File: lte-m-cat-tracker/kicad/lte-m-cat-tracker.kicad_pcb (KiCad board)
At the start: 2 copper layers, 30 x 35 mm, 33 parts, among them J1 JST-GH-1.25mm-2P, J2 USB-C-16P, SW1 MSK12C02, U1 SIM7080G-M, U2 ESP32-C3, U3 LIS2DW12TR, U4 TP4056, U5 XC6220B331MR-G

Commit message: STEP4a: ANT3→C127629(1206)・C13→C49326798・BOM/CPL作成（2026-06-07）
Co-Authored-By: Claude Sonnet 4.6 <noreply@anthropic.com>
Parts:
- ANT3: value 2450AT18A100 -> RFANT3216120A5T; footprint (none) -> ChipAntenna_1206
- moved ANT3 3.51 mm to (1.80, 19.0)
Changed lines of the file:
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@@
 		(embedded_fonts no)
 	)
-	(footprint ""
+	(footprint "ChipAntenna_1206"
 		(layer "F.Cu")
-		(at 2 22.5)
+		(at 1.8 19.0)
 		(property "Reference" "ANT3"
-			(at 0 -3.5 0)
+			(at 0 -2.0 0)
 			(layer "F.SilkS")
 			(effects
@@
 			)
 		)
-		(property "Value" "2450AT18A100"
-			(at 0 3.5 0)
+		(property "Value" "RFANT3216120A5T"
+			(at 0 2.0 0)
 			(layer "F.Fab")
 			(effects
@@
 			)
 		)
-		(property "Description" ""
+		(property "Description" "2.4GHz chip antenna 1206 Walsin RFANT3216120A5T"
 			(at 0 0 0)
 			(layer "F.Fab")
@@
 		)
 		(duplicate_pad_numbers_are_jumpers no)
-		(fp_line
-			(start -0.2 -0.6)
-			(end -0.2 0.6)
-			(stroke
-				(width 0.12)
-				(type default)
-			)
-			(layer "F.SilkS")
-		)
 		(fp_rect
-			(start -1.2 -0.8)
-			(end 1.2 0.8)
+			(start -1.8 -1.0)
+			(end 1.8 1.0)
 			(stroke
 				(width 0.05)
@@
 		)
 		(fp_rect
-			(start -1 -0.625)
-			(end 1 0.625)
+			(start -1.6 -0.8)
+			(end 1.6 0.8)
 			(stroke
 				(width 0.1)
@@
 		)
 		(pad "1" smd rect
-			(at -0.5 0)
-			(size 0.8 1.25)
+			(at -1.3 0)
+			(size 1.6 1.8)
 			(layers "F.Cu" "F.Mask" "F.Paste")
 			(net "WIFI_ANT")
@@
 		)
 		(pad "2" smd rect
-			(at 0.5 0)
-			(size 0.8 1.25)
+			(at 1.3 0)
+			(size 1.6 1.8)
 			(layers "F.Cu" "F.Mask" "F.Paste")
 			(net "GND")

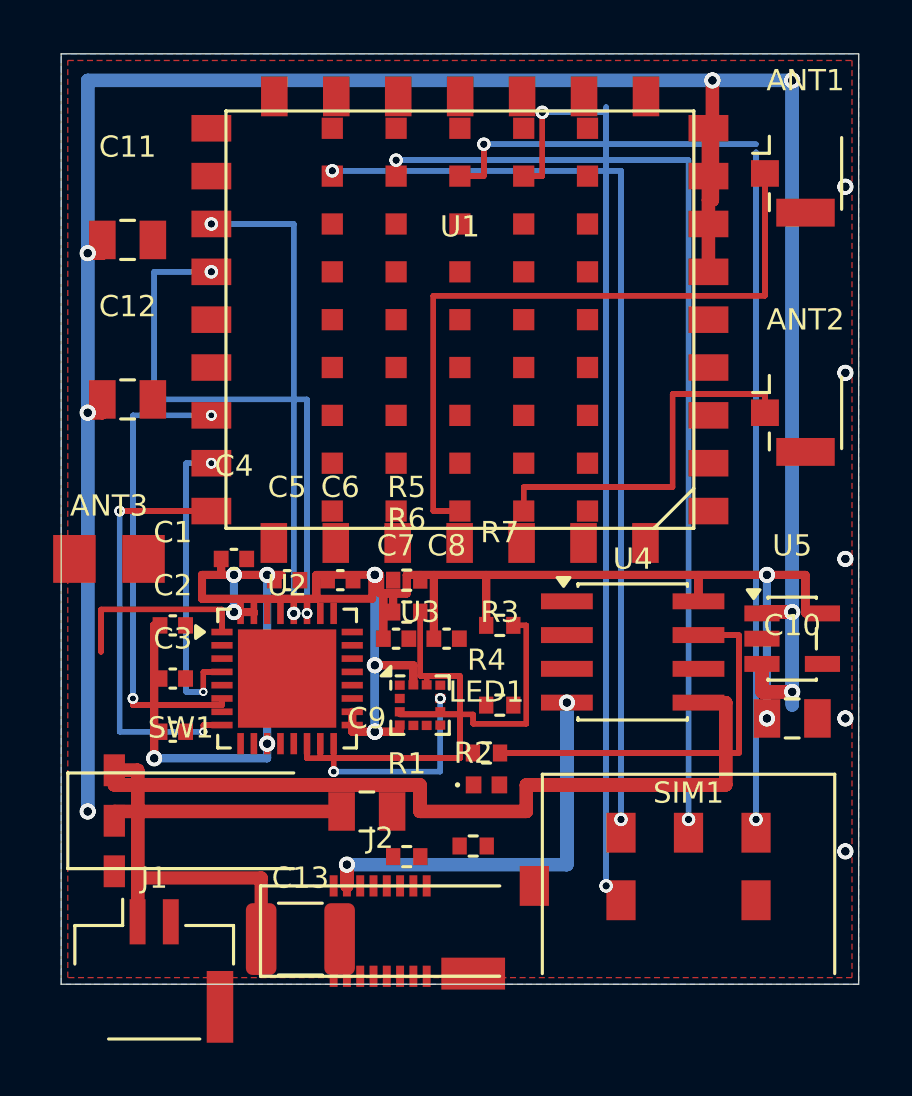
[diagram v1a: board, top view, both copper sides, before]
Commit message: route_pcb_v10.py: +3.3Vバスバイパス y=20.5→y=20.4に修正（短絡0件）
- y=20.5ではU2.pad25/26(y_min=20.65)にtrace y_max=20.65で接触（0mm）
- y=20.4に変更: trace y_max=20.55, pad y_min=20.65 → gap=0.10mm ✅
- y=18.5上方迂回案はU1底行パッド(y=18.4)に接触するため採用不可と判明
- DRC結果: 短絡0件 ✅ / 未配線44件

Co-Authored-By: Claude Sonnet 4.6 <noreply@anthropic.com>
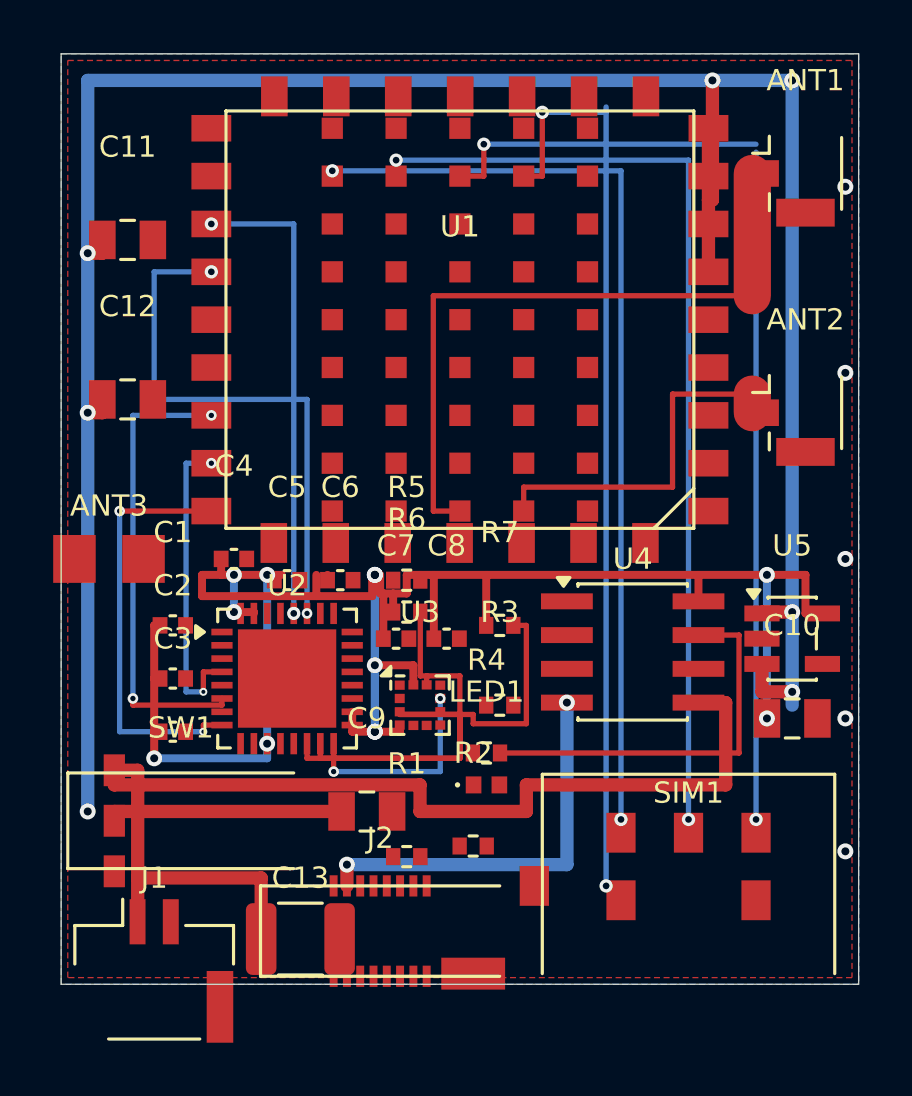
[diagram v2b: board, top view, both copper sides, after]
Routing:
- net VBAT_SW: track 203.8 -> 101.9 mm, vias 14 -> 7
- net +3.3V: track 163.6 -> 82.0 mm, vias 24 -> 12
- net SIM_CLK: track 75.9 -> 37.9 mm, vias 4 -> 2
- net SIM_DATA: track 73.8 -> 36.9 mm, vias 4 -> 2
- net VBAT: track 79.5 -> 43.2 mm
- net SIM_VDD: track 71.9 -> 36.0 mm, vias 4 -> 2
- net SIM_RST: track 71.8 -> 35.9 mm, vias 4 -> 2
- net LTE_ANT: track 52.4 -> 25.7 mm
- net SIM_TXD: track 41.5 -> 20.8 mm, vias 4 -> 2
- net I2C_SCL: track 38.2 -> 19.1 mm
- net SIM_RXD: track 35.5 -> 17.8 mm, vias 4 -> 2
- net SIM_RESETN: track 34.9 -> 17.5 mm, vias 4 -> 2
- net SIM_PWRKEY: track 31.7 -> 15.8 mm, vias 4 -> 2
- net VUSB: track 30.3 -> 15.2 mm, vias 4 -> 2
- net CHRG: track 29.9 -> 14.9 mm
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
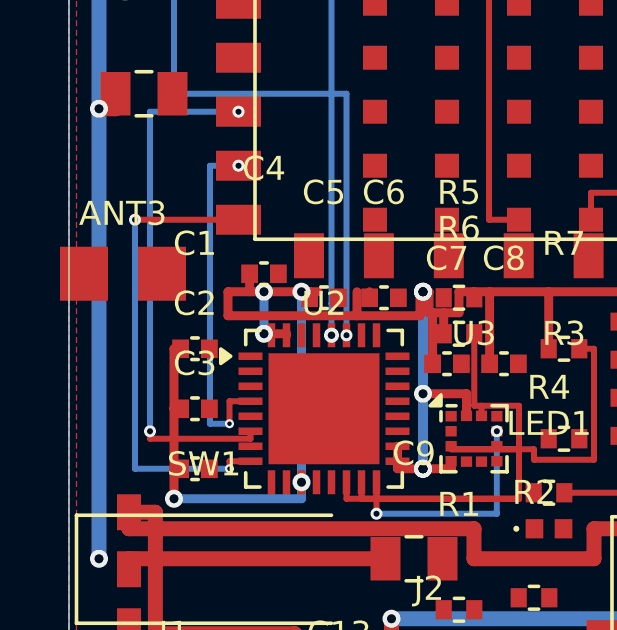
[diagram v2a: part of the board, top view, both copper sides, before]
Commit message: WIFI_ANT配線完了: U2.pad1→ANT3.pad1 F.Cu 0.2mm（短絡0件 ✅ / 未配線10件）
Co-Authored-By: Claude Sonnet 4.6 <noreply@anthropic.com>
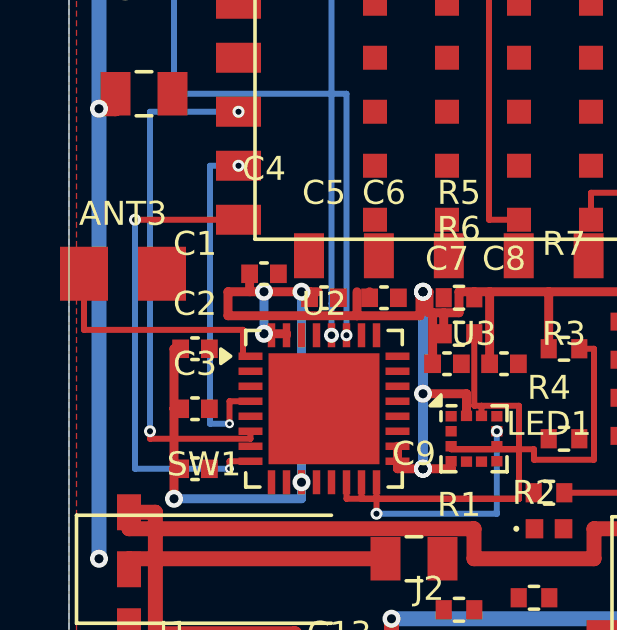
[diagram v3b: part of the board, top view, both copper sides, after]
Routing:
- net WIFI_ANT: track 0.00 -> 8.30 mm
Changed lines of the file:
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@@
 	(segment (start 23.0 12.8) (end 26.0 12.8) (width 0.2) (layer "F.Cu") (net "GNSS_ANT"))
 	(segment (start 26.0 12.8) (end 26.0 13.5) (width 1.4) (layer "F.Cu") (net "GNSS_ANT"))
+	(segment (start 6.05 21.75) (end 5.8 21.75) (width 0.2) (layer "F.Cu") (net "WIFI_ANT"))
+	(segment (start 5.8 21.75) (end 5.8 20.87) (width 0.2) (layer "F.Cu") (net "WIFI_ANT"))
+	(segment (start 5.8 20.87) (end 0.5 20.87) (width 0.2) (layer "F.Cu") (net "WIFI_ANT"))
+	(segment (start 0.5 20.87) (end 0.5 19.0) (width 0.2) (layer "F.Cu") (net "WIFI_ANT"))
 	(zone
 		(net "GND")

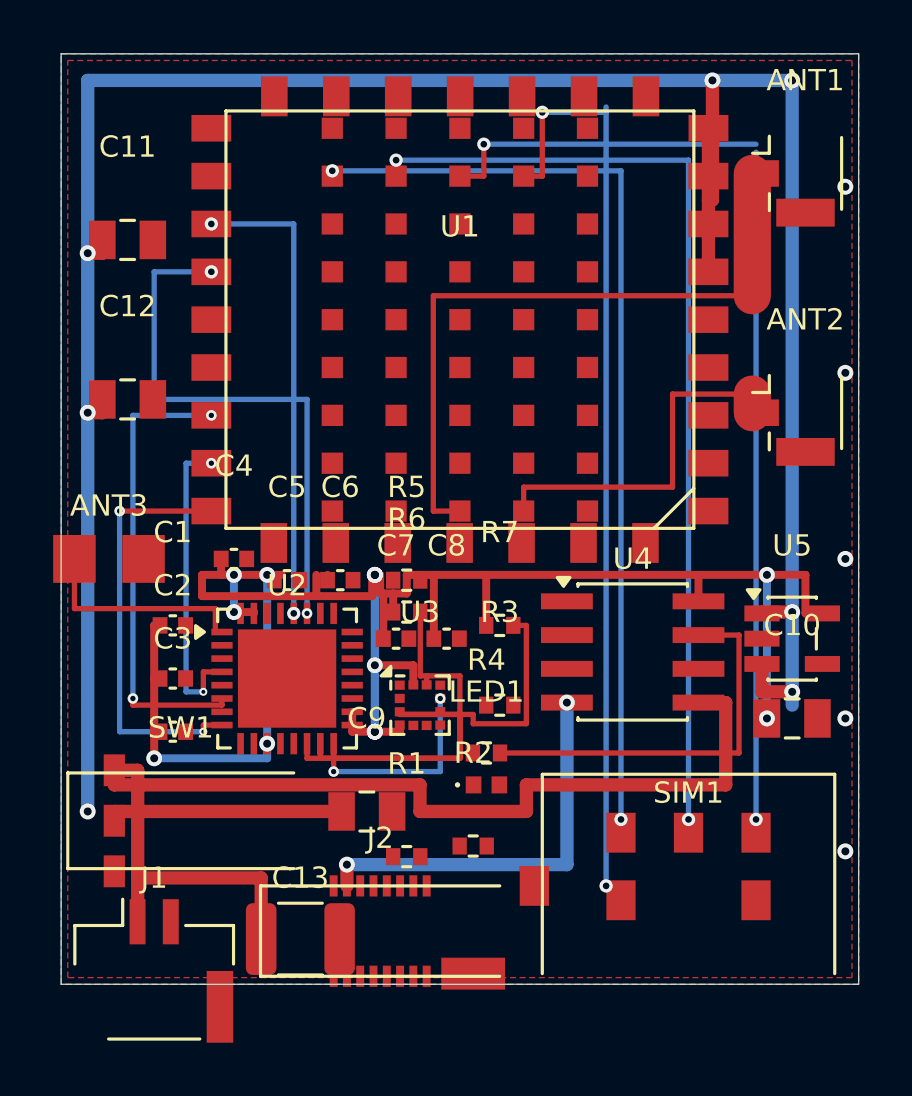
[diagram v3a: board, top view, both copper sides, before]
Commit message: 追加配線: SIM_CLK gap・U2 pad2/3・U3 pad2 (+3.3V) → 短絡0件 / 未配線6件(全GND zone)
Co-Authored-By: Claude Sonnet 4.6 <noreply@anthropic.com>
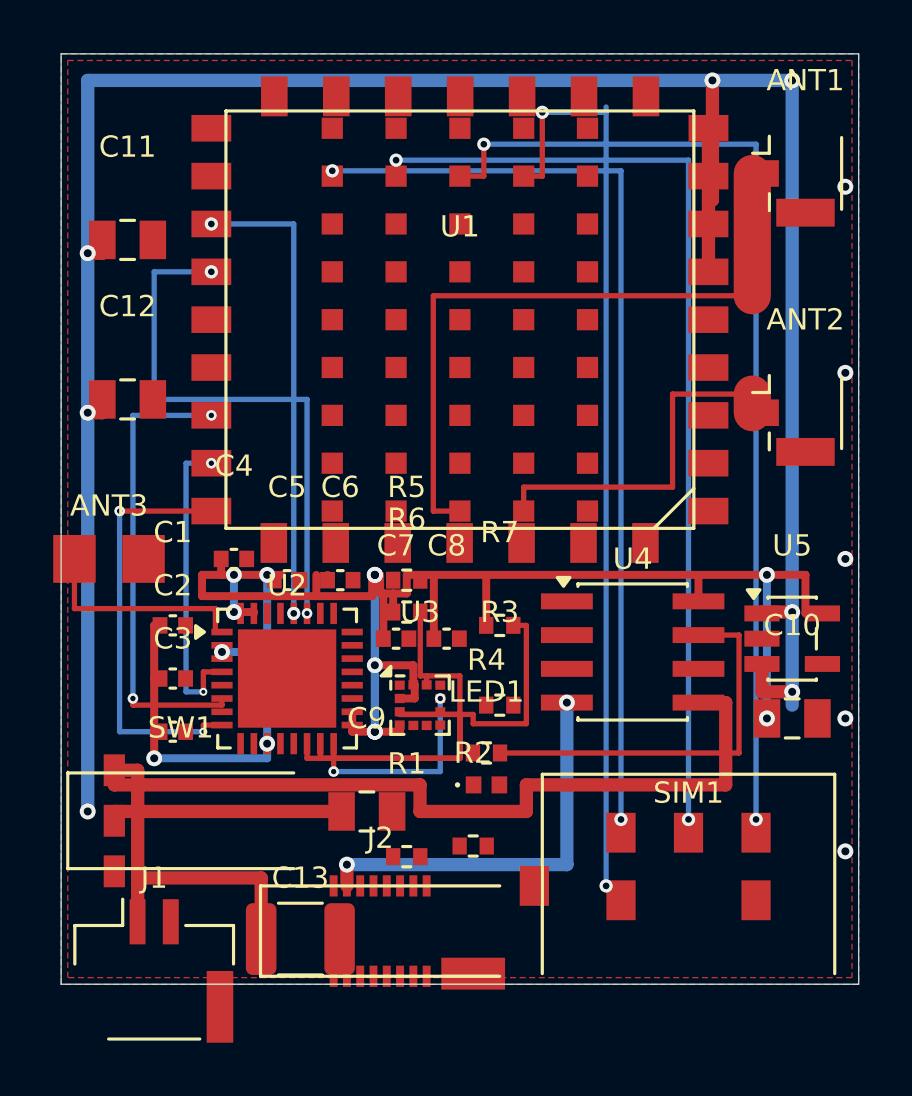
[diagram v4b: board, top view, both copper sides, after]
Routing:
- net +3.3V: track 82.0 -> 84.8 mm, vias 12 -> 13
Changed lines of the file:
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@@
 	(segment (start 5.8 20.87) (end 0.5 20.87) (width 0.2) (layer "F.Cu") (net "WIFI_ANT"))
 	(segment (start 0.5 20.87) (end 0.5 19.0) (width 0.2) (layer "F.Cu") (net "WIFI_ANT"))
+	(segment (start 26.14 3.4) (end 26.14 3.7) (width 0.2) (layer "B.Cu") (net "SIM_CLK"))
+	(via (at 6.05 22.5) (size 0.6) (drill 0.3) (layers "F.Cu" "B.Cu") (net "+3.3V"))
+	(segment (start 6.05 22.5) (end 7.75 22.5) (width 0.3) (layer "B.Cu") (net "+3.3V"))
+	(segment (start 13.25 23.738) (end 13.3 23.738) (width 0.3) (layer "F.Cu") (net "+3.3V"))
+	(segment (start 13.3 23.738) (end 13.3 24.25) (width 0.3) (layer "F.Cu") (net "+3.3V"))
+	(segment (start 13.3 24.25) (end 12.7375 24.25) (width 0.3) (layer "F.Cu") (net "+3.3V"))
 	(zone
 		(net "GND")

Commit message: SIM_RST B.Cu x=20.5→x=27.0へ迂回（crosses_crossing 8→5件）
Co-Authored-By: Claude Sonnet 4.6 <noreply@anthropic.com>
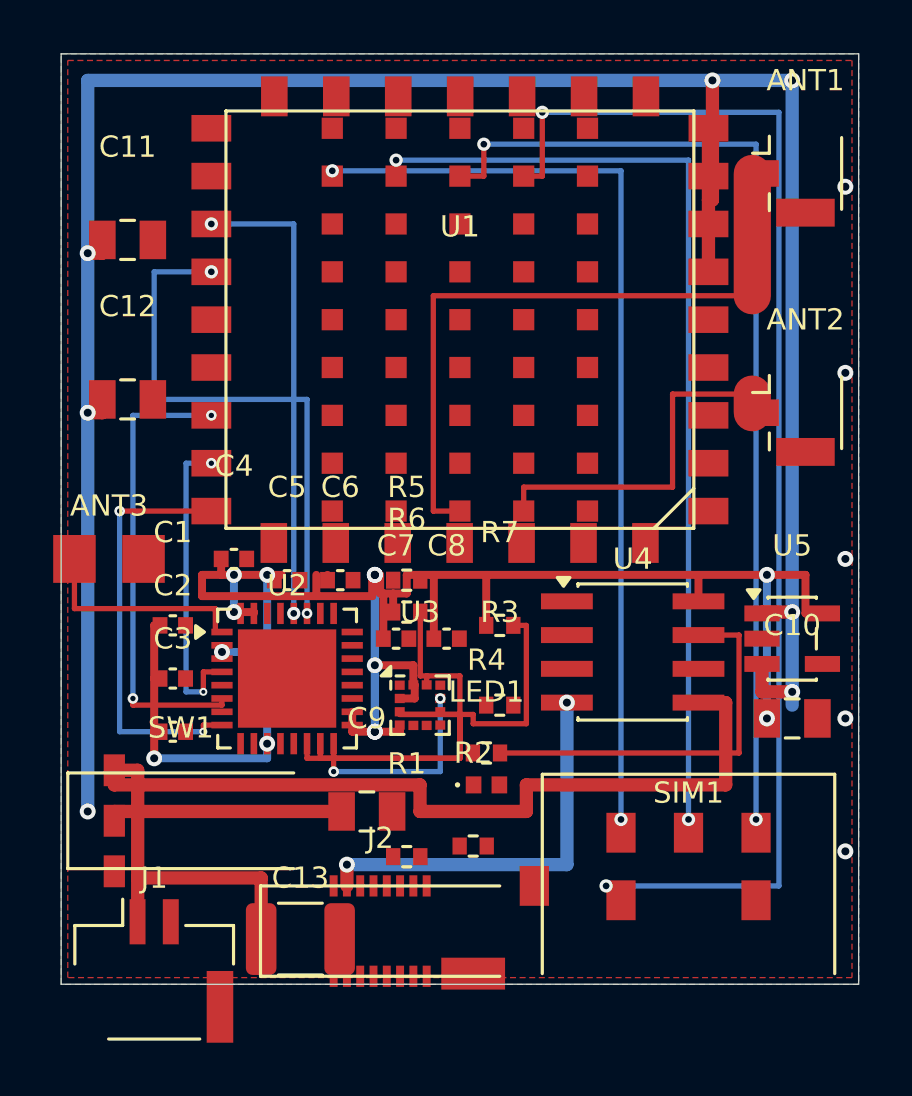
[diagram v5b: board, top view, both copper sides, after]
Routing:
- net SIM_RST: track 35.9 -> 48.7 mm
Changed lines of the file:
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@@
 	(segment (start 18.1 4.6) (end 18.1 2.2) (width 0.2) (layer "F.Cu") (net "SIM_RST"))
 	(via (at 18.1 2.2) (size 0.5) (drill 0.25) (layers "F.Cu" "B.Cu") (net "SIM_RST"))
-	(segment (start 18.1 2.2) (end 20.5 2.2) (width 0.2) (layer "B.Cu") (net "SIM_RST"))
-	(segment (start 20.5 2.0) (end 20.5 31.3) (width 0.2) (layer "B.Cu") (net "SIM_RST"))
+	(segment (start 18.1 2.2) (end 27.0 2.2) (width 0.2) (layer "B.Cu") (net "SIM_RST"))
+	(segment (start 27.0 2.2) (end 27.0 31.3) (width 0.2) (layer "B.Cu") (net "SIM_RST"))
+	(segment (start 27.0 31.3) (end 20.5 31.3) (width 0.2) (layer "B.Cu") (net "SIM_RST"))
 	(via (at 20.5 31.3) (size 0.5) (drill 0.25) (layers "F.Cu" "B.Cu") (net "SIM_RST"))
 	(segment (start 20.5 31.3) (end 21.06 31.3) (width 0.2) (layer "F.Cu") (net "SIM_RST"))
